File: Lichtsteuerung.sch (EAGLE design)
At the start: 180 parts, among them IC1 74HC595D, IC10 TSR_1-2450, IC11 MEGA64-A, IC12 75176AD, IC13 DS1307SO8, IC2 74HC595D, IC3 74HC595D, IC4 74HC595D, IC5 75176AD, IC6 MEGA8-AI, IC9 24FC128-I/SN, Q1 32.768, Q2 16MHz, Q3 16MHz, U1 MAX232SOIC16, X1 713-1410, X2 713-1410, X3 733-333, X5 713-1410, X6 733-334, X7 733-333, X8 733-333

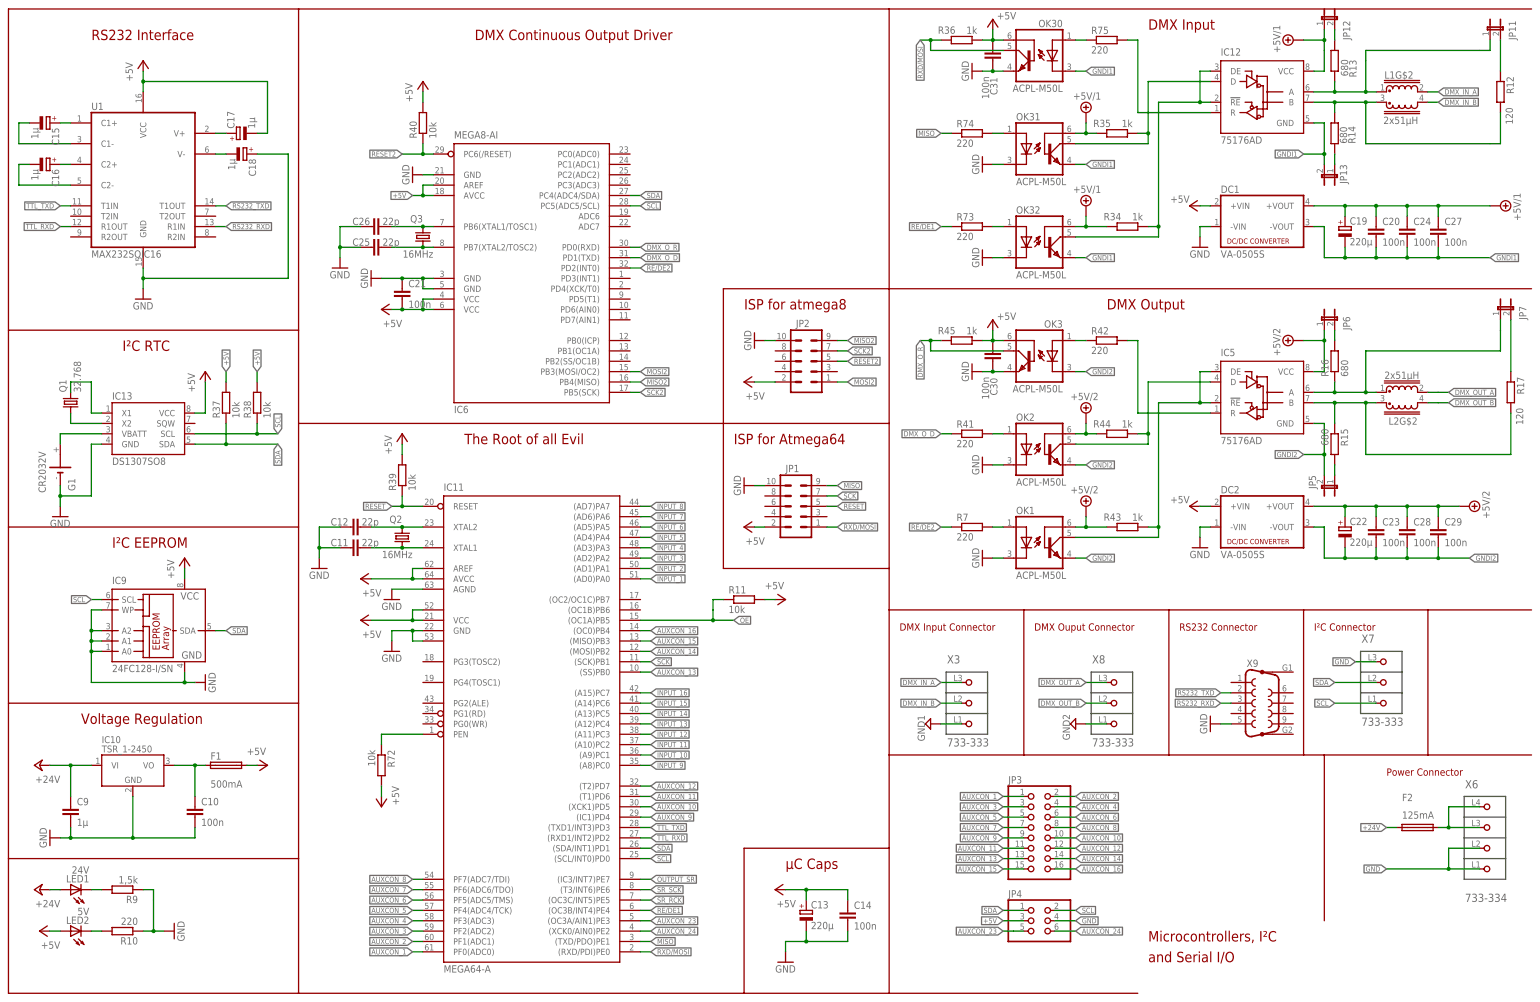
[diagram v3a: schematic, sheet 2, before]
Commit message: Re-added smd jumpers, fixed silkscreens and added a few test points
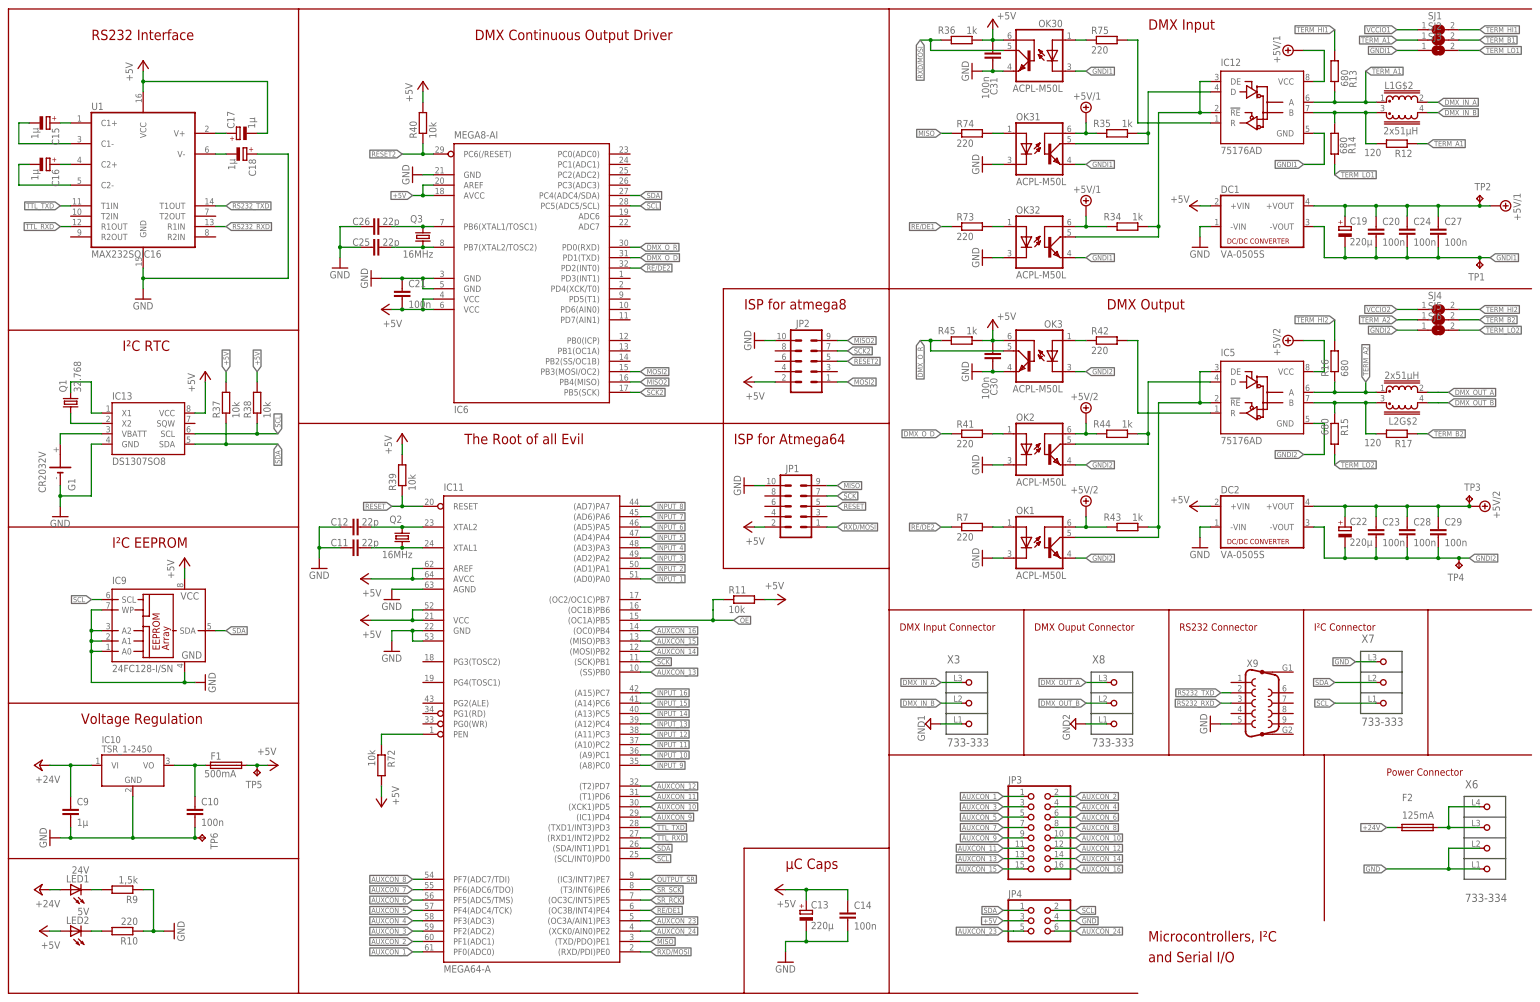
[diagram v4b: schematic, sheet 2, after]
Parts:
- removed JP11, JP12, JP13, JP5, JP6, JP7: (no value), SparkFun:JUMPER-2SMD-NC
- added SJ1, SJ2, SJ3, SJ4, SJ5, SJ6: (no value), jumper:SJ
- added TP1, TP2, TP3, TP4, TP5, TP6: TPPAD1-13, testpad:TPPAD1-13
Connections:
- removed net N$53: IC12.A, JP11.1, L1G$1.1, R13.1
- removed net N$77: IC5.A, JP7.1, L2G$1.1, R16.1
- removed net N$85: JP12.2, R13.2
- removed net N$86: JP13.1, R14.1
- removed net N$89: JP11.2, R12.1
- removed net N$91: JP5.1, R15.2
- removed net N$92: JP7.2, R17.1
- removed net N$94: JP6.2, R16.2
- new net TERM_A1: IC12.A, L1G$1.1, R12.1, R13.1, SJ2.1
- new net TERM_A2: IC5.A, L2G$1.1, R16.1, SJ5.1
- new net TERM_B1: SJ2.2
- new net TERM_B2: R17.1, SJ5.2
- new net TERM_HI1: R13.2, SJ1.2
- new net TERM_HI2: R16.2, SJ4.2
- new net TERM_LO1: R14.1, SJ3.2
- new net TERM_LO2: R15.2, SJ6.2
- net +5V: now also TP5.TP
- net GND: now also TP6.TP
- net GNDI1: now also SJ3.1, TP1.TP; no longer JP13.2
- net GNDI2: now also SJ6.1, TP4.TP; no longer JP5.2
- net VCCIO1: now also SJ1.1, TP2.TP; no longer JP12.1
- net VCCIO2: now also SJ4.1, TP3.TP; no longer JP6.1
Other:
- moved on the sheet: IC12, L1G$2, R12, R13, R14, R15, R17

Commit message: Added reichelt ordercodes
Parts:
- C10, C14, C20, C21, C23, C24, C27, C28, C29, C30, C31: OC_REICHELT (none) -> X7R-G0805 100N
- C11, C12, C25, C26: OC_REICHELT (none) -> X7R-G0805 22P
- C13: OC_REICHELT (none) -> VF 220/6,3 K-D
- C15, C16, C17, C18: OC_REICHELT (none) -> VF 1,0/50 C-B
- C9: OC_REICHELT (none) -> X7R-G0805 1,0/50
- DC1, DC2: OC_REICHELT (none) -> SIM1-0505 SIL4
- F1: OC_REICHELT (none) -> SMD-HASF 0,5A
- F2: OC_REICHELT (none) -> SMD-HASF 0,25A
- F3, F4, F5: OC_REICHELT (none) -> PTC194600-050
- G1: OC_REICHELT (none) -> KZH 20PCB-V
- IC10: OC_REICHELT (none) -> TSR 1-2450
- IC11: OC_REICHELT (none) -> ATMEGA 64-16 TQ
- IC12, IC5: OC_REICHELT (none) -> SN 75176BD
- IC13: OC_REICHELT (none) -> DS 1307Z
- IC6: OC_REICHELT (none) -> ATMEGA 8A-AU
- IC9: OC_REICHELT (none) -> 24FC128-I/SN
- JP1, JP2: OC_REICHELT (none) -> WSL 10G
- JP3: OC_REICHELT (none) -> MPE 087-2-016
- JP4: OC_REICHELT (none) -> MPE 087-2-006
- L1, L2: OC_DIGIKEY (none) -> 495-1868-1-ND
- LED1: OC_REICHELT (none) -> SMD-LED 0805 RT
- LED2: OC_REICHELT (none) -> SMD-LED 0805 GE
- OK1, OK2, OK3, OK30, OK31, OK32: OC_DIGIKEY (none) -> 516-2166-5-ND
- Q1: OC_REICHELT (none) -> 0,032768-SMD
- Q2, Q3: OC_REICHELT (none) -> 16,000000-MJ
- R10, R41, R42, R7, R73, R74, R75: OC_REICHELT (none) -> SMD-0805 220
- R101, R102, R103, R104, R105, R106, R107, R108, R109, R110, R111, R112, R113, R114, R115, R116: OC_REICHELT (none) -> SMD-0805 1,20K
- R11, R201, R202, R203, R204, R205, R206, R207, R208, R209, R210, R211, R212, R213, R214, R215, R216, R221, R222, R223, R224, R225, R226, R227, R228, R229, R230, R231, R232, R233, R234, R235, R236, R37, R38, R39, R40, R72: OC_REICHELT (none) -> SMD-0805 10,0K
- R12, R17: OC_REICHELT (none) -> SMD-0805 120
- R13, R14, R15, R16: OC_REICHELT (none) -> SMD-0805 680
- R34, R35, R36, R43, R44, R45: OC_REICHELT (none) -> SMD-0805 1,00K
- R9: OC_REICHELT (none) -> SMD-0805 1,50K
- U1: OC_REICHELT (none) -> MAX 232 CSE SMD
- X1, X2, X5: OC_REICHELT (none) -> WAGO 713-1410
- X3, X7, X8: OC_REICHELT (none) -> WAGO 733-333
- X6: OC_REICHELT (none) -> WAGO 733-334
- X9: OC_REICHELT (none) -> D-SUB BU 09P
- renumbered R18 to R229, R19 to R230, R20 to R231, R21 to R232, R22 to R233, R23 to R234, R24 to R235, R25 to R236, R26 to R228, R27 to R227, R28 to R226, R29 to R225, R30 to R224, R31 to R223, R32 to R222, R33 to R221

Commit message: Fake commit to test the board gen hook
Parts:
- C21: OC_FOO (none) -> test
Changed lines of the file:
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@@
 </part>
 <part name="C21" library="resistor" deviceset="C-EU" device="C0805" value="100n">
+<attribute name="OC_FOO" value="test"/>
 <attribute name="OC_REICHELT" value="X7R-G0805 100N"/>
 </part>
@@
 <attribute name="VALUE" x="347.472" y="160.02" size="1.778" layer="96" rot="MR180"/>
 </instance>
-<instance part="C21" gate="G$1" x="106.68" y="180.34">
+<instance part="C21" gate="G$1" x="106.68" y="180.34" smashed="yes">
 <attribute name="OC_REICHELT" x="106.68" y="180.34" size="1.778" layer="96" display="off"/>
+<attribute name="NAME" x="108.204" y="180.721" size="1.778" layer="95"/>
+<attribute name="VALUE" x="108.204" y="175.641" size="1.778" layer="96"/>
+<attribute name="OC_FOO" x="106.68" y="180.34" size="1.778" layer="96" display="off"/>
 </instance>
 <instance part="JP4" gate="A" x="261.62" y="25.4">

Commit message: Another hook test
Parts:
- C21: OC_FOO test -> (none)
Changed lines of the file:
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@@
 </part>
 <part name="C21" library="resistor" deviceset="C-EU" device="C0805" value="100n">
-<attribute name="OC_FOO" value="test"/>
 <attribute name="OC_REICHELT" value="X7R-G0805 100N"/>
 </part>
@@
 <attribute name="NAME" x="108.204" y="180.721" size="1.778" layer="95"/>
 <attribute name="VALUE" x="108.204" y="175.641" size="1.778" layer="96"/>
-<attribute name="OC_FOO" x="106.68" y="180.34" size="1.778" layer="96" display="off"/>
 </instance>
 <instance part="JP4" gate="A" x="261.62" y="25.4">

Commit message: Final hook test, seems to work
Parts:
- C21: OC_FELIFAIL (none) -> I SHOULD READ INSTRUCTIONS MORE CAREFULLY.
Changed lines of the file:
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@@
 </part>
 <part name="C21" library="resistor" deviceset="C-EU" device="C0805" value="100n">
+<attribute name="OC_FELIFAIL" value="I SHOULD READ INSTRUCTIONS MORE CAREFULLY."/>
 <attribute name="OC_REICHELT" value="X7R-G0805 100N"/>
 </part>
@@
 <attribute name="NAME" x="108.204" y="180.721" size="1.778" layer="95"/>
 <attribute name="VALUE" x="108.204" y="175.641" size="1.778" layer="96"/>
+<attribute name="OC_FELIFAIL" x="106.68" y="180.34" size="1.778" layer="96" display="off"/>
 </instance>
 <instance part="JP4" gate="A" x="261.62" y="25.4">
